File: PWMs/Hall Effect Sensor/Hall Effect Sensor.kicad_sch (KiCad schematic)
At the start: 5 parts, among them J1 PH1-20-UA, J2 PH1-20-UA

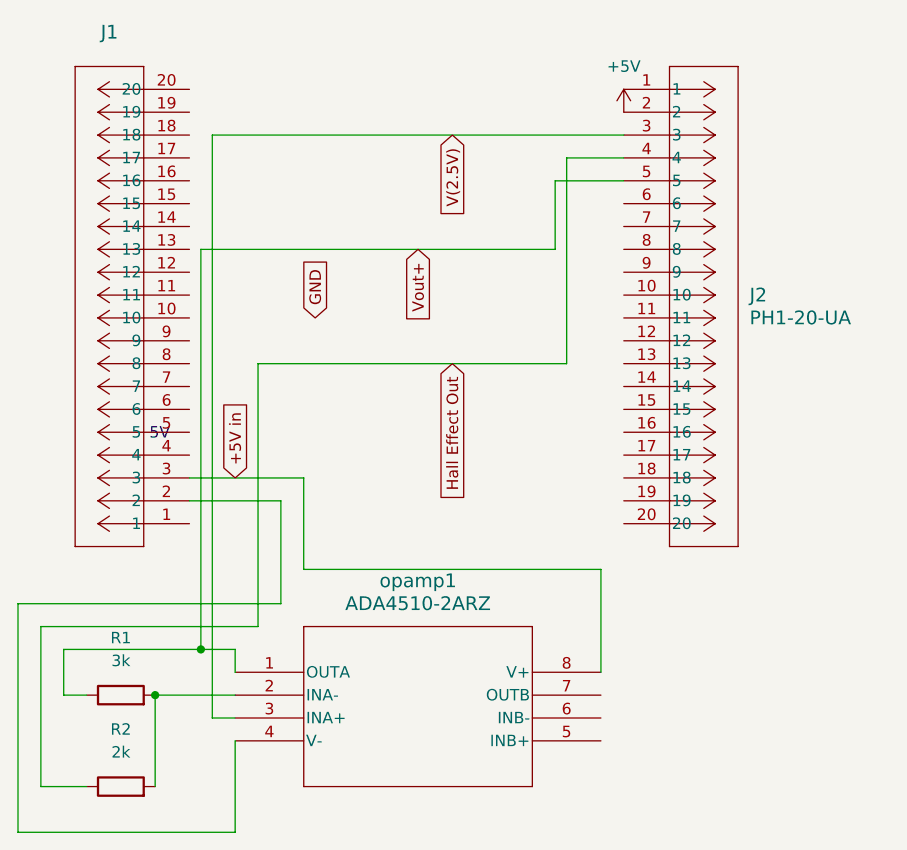
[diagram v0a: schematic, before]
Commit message: Hall Effect Board Changes
Added a voltage divider to get to 2.5V, as there is not a VCU output which can do that - its toggleable by jumper cable, so if we have a better solution we don't need to make a new board to implement it.
Also moved pins to all be in the same row, since most of our boards are designed like that and it makes the overall board slightly less messy.
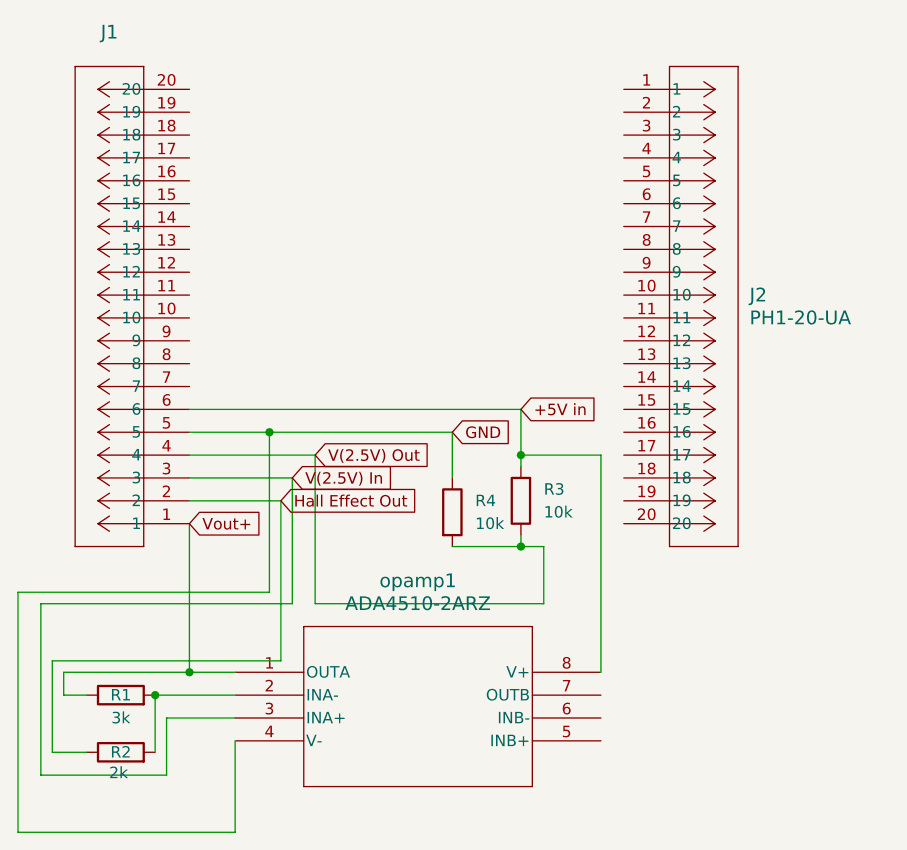
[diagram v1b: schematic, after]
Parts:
- added R3, R4: 10k, Resistor_THT:R_Axial_DIN0207_L6.3mm_D2.5mm_P10.16mm_Horizontal, symbol Device:R
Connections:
- net +5V in: now also J1.6, R3.2; no longer J1.3
- net GND: now also J1.5, opamp1.4 (V-), R4.1
- net Hall Effect Out: now also J1.2; no longer J2.4
- net Vout+: now also J1.1; no longer J2.5
- net V(2.5V) Out: now reaches J1.4
- net V(2.5V) Out: now also R3.1, R4.2
- net +5V: no longer names the net of J2.2
- net V(2.5V): no longer names the net of J2.3
- net V(2.5V): no longer opamp1.3 (INA+)
- new net V(2.5V) In: J1.3, opamp1.3 (INA+)
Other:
- note removed: "5V"
- moved on the sheet: R2
